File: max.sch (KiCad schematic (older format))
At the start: 48 parts, among them P4 ttyMAX2, P5 ttyMAX1, P6 ttyMAX0, SW2 gpio 8 9 10 11, U8 SG-210STF_16MHz, U9 MAX14830

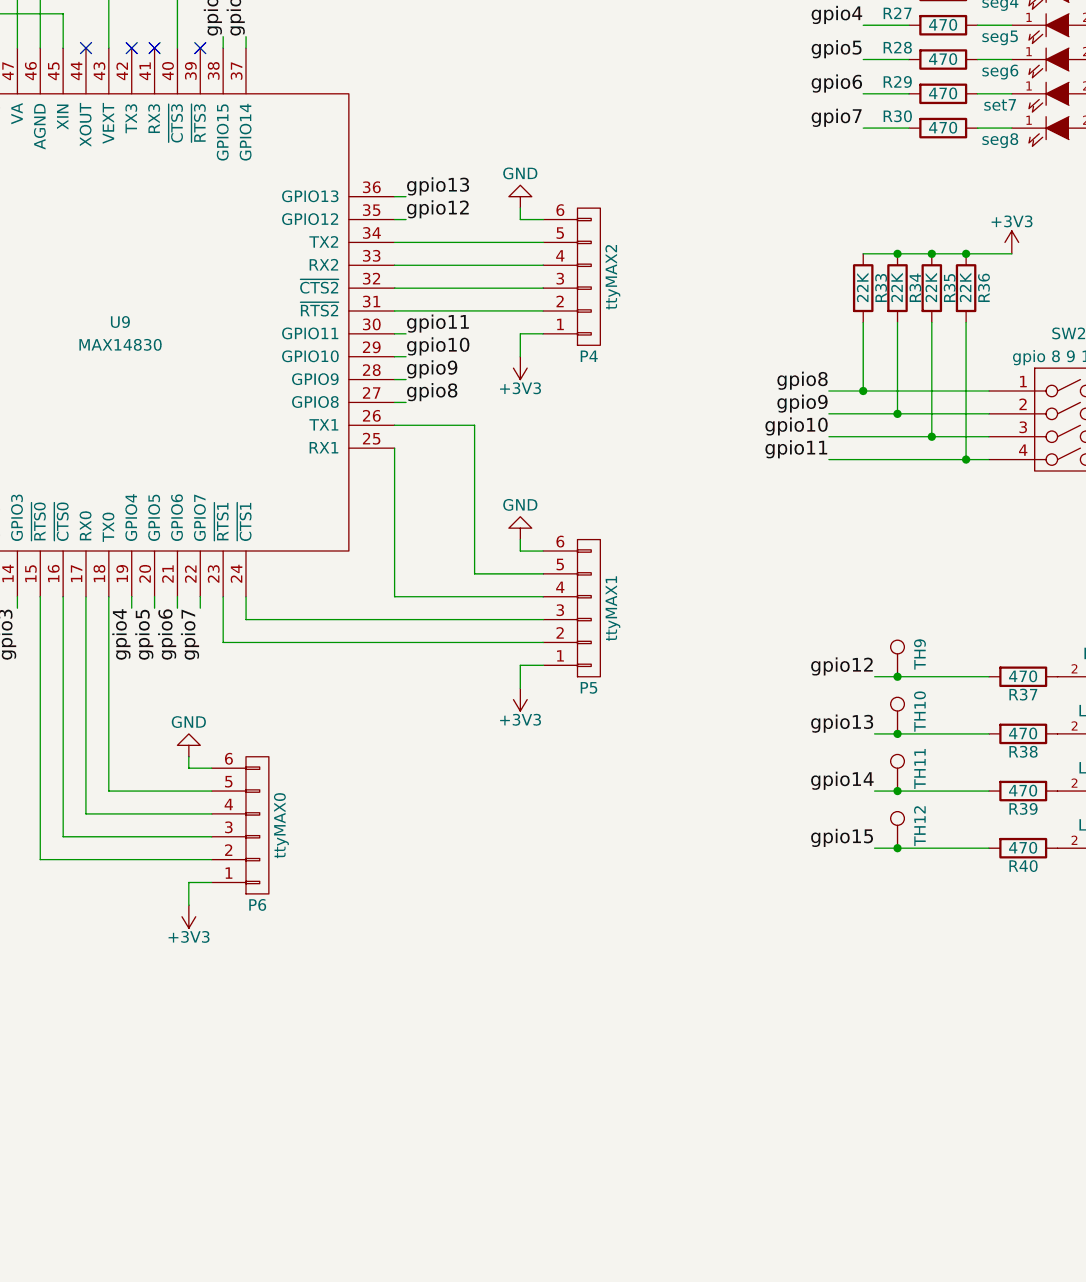
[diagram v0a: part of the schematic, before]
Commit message: Improved the pin comatibility to match with other ardupilot project.
Signed-off-by: Akira Tsukamoto <akira-t@s9.dion.ne.jp>
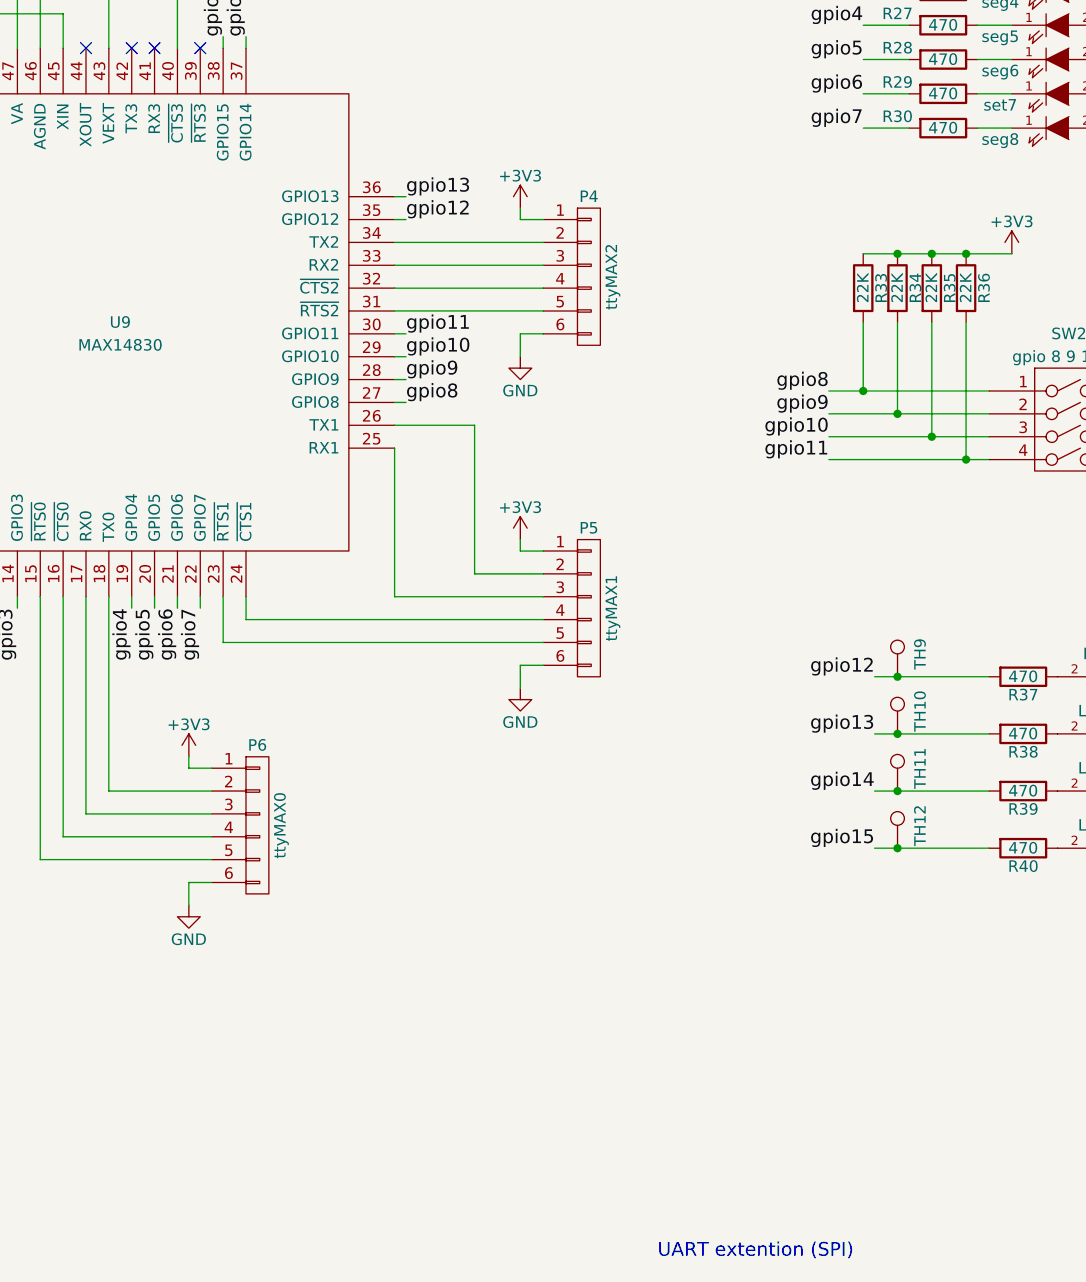
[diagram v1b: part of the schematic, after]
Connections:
- net at U9.15 (~RTS0): now also P6.5 (P5); no longer P6.2 (P2)
- net at U9.16 (~CTS0): now also P6.4 (P4); no longer P6.3 (P3)
- net at U9.17 (RX0): now also P6.3 (P3); no longer P6.4 (P4)
- net at U9.18 (TX0): now also P6.2 (P2); no longer P6.5 (P5)
- net at U9.23 (~RTS1): now also P5.5 (P5); no longer P5.2 (P2)
- net at U9.24 (~CTS1): now also P5.4 (P4); no longer P5.3 (P3)
- net at U9.25 (RX1): now also P5.3 (P3); no longer P5.4 (P4)
- net at U9.26 (TX1): now also P5.2 (P2); no longer P5.5 (P5)
- net at U9.31 (~RTS2): now also P4.5 (P5); no longer P4.2 (P2)
- net at U9.32 (~CTS2): now also P4.4 (P4); no longer P4.3 (P3)
- net at U9.33 (RX2): now also P4.3 (P3); no longer P4.4 (P4)
- net at U9.34 (TX2): now also P4.2 (P2); no longer P4.5 (P5)
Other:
- note added: "UART extention (SPI)"
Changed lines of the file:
@@
 F 3 "" H 7000 3200 60  0000 C CNN
 	1    7000 3200
-	1    0    0    1
+	1    0    0    -1
 $EndComp
 $Comp
 L GND #PWR042
 U 1 1 56F7B7A9
-P 6700 2900
-F 0 "#PWR042" H 6700 2650 50  0001 C CNN
-F 1 "GND" H 6700 2750 50  0000 C CNN
-F 2 "" H 6700 2900 60  0000 C CNN
-F 3 "" H 6700 2900 60  0000 C CNN
-	1    6700 2900
-	1    0    0    1
+P 6700 3550
+F 0 "#PWR042" H 6700 3300 50  0001 C CNN
+F 1 "GND" H 6700 3400 50  0000 C CNN
+F 2 "" H 6700 3550 60  0000 C CNN
+F 3 "" H 6700 3550 60  0000 C CNN
+	1    6700 3550
+	-1   0    0    -1
 $EndComp
 $Comp
@@
 F 3 "" H 7000 4650 60  0000 C CNN
 	1    7000 4650
-	1    0    0    1
+	1    0    0    -1
 $EndComp
 $Comp
 L GND #PWR043
 U 1 1 56F7B7BC
-P 6700 4350
-F 0 "#PWR043" H 6700 4100 50  0001 C CNN
-F 1 "GND" H 6700 4200 50  0000 C CNN
-F 2 "" H 6700 4350 60  0000 C CNN
-F 3 "" H 6700 4350 60  0000 C CNN
-	1    6700 4350
-	1    0    0    1
+P 6700 5000
+F 0 "#PWR043" H 6700 4750 50  0001 C CNN
+F 1 "GND" H 6700 4850 50  0000 C CNN
+F 2 "" H 6700 5000 60  0000 C CNN
+F 3 "" H 6700 5000 60  0000 C CNN
+	1    6700 5000
+	-1   0    0    -1
 $EndComp
 $Comp
@@
 F 3 "" H 5550 5600 60  0000 C CNN
 	1    5550 5600
-	1    0    0    1
-$EndComp
-$Comp
-L GND #PWR044
-U 1 1 56F7B7CF
-P 5250 5300
-F 0 "#PWR044" H 5250 5050 50  0001 C CNN
-F 1 "GND" H 5250 5150 50  0000 C CNN
-F 2 "" H 5250 5300 60  0000 C CNN
-F 3 "" H 5250 5300 60  0000 C CNN
-	1    5250 5300
-	1    0    0    1
+	1    0    0    -1
 $EndComp
 Text HLabel 1950 3050 0    60   Output ~ 0
@@
 $EndComp
 $Comp
-L GND #PWR045
+L GND #PWR044
 U 1 1 56FF154F
 P 9450 6000
-F 0 "#PWR045" H 9450 5750 50  0001 C CNN
+F 0 "#PWR044" H 9450 5750 50  0001 C CNN
 F 1 "GND" H 9450 5850 50  0000 C CNN
 F 2 "" H 9450 6000 60  0000 C CNN
@@
 $EndComp
 $Comp
-L GND #PWR046
+L GND #PWR045
 U 1 1 56FF190C
 P 9450 4450
-F 0 "#PWR046" H 9450 4200 50  0001 C CNN
+F 0 "#PWR045" H 9450 4200 50  0001 C CNN
 F 1 "GND" H 9450 4300 50  0000 C CNN
 F 2 "" H 9450 4450 60  0000 C CNN
@@
 NoConn ~ 4800 2200
 $Comp
-L GND #PWR047
+L GND #PWR046
 U 1 1 56FEE288
 P 3200 2250
-F 0 "#PWR047" H 3200 2000 50  0001 C CNN
+F 0 "#PWR046" H 3200 2000 50  0001 C CNN
 F 1 "GND" H 3200 2100 50  0000 C CNN
 F 2 "" H 3200 2250 50  0000 C CNN
@@
 $EndComp
 $Comp
-L GND #PWR048
+L GND #PWR047
 U 1 1 5705B8B8
 P 3750 2500
-F 0 "#PWR048" H 3750 2250 50  0001 C CNN
+F 0 "#PWR047" H 3750 2250 50  0001 C CNN
 F 1 "GND" H 3750 2350 50  0000 C CNN
 F 2 "" H 3750 2500 60  0000 C CNN
@@
 $EndComp
 $Comp
-L GND #PWR049
+L GND #PWR048
 U 1 1 57061BCC
 P 2900 4100
-F 0 "#PWR049" H 2900 3850 50  0001 C CNN
+F 0 "#PWR048" H 2900 3850 50  0001 C CNN
 F 1 "GND" H 2900 3950 50  0000 C CNN
 F 2 "" H 2900 4100 60  0000 C CNN
@@
 $EndComp
 $Comp
-L GND #PWR050
+L GND #PWR049
 U 1 1 57063190
 P 4300 1800
-F 0 "#PWR050" H 4300 1550 50  0001 C CNN
+F 0 "#PWR049" H 4300 1550 50  0001 C CNN
 F 1 "GND" H 4300 1650 50  0000 C CNN
 F 2 "" H 4300 1800 60  0000 C CNN
@@
 $EndComp
 $Comp
-L GND #PWR051
+L GND #PWR050
 U 1 1 5706380D
 P 4750 1800
-F 0 "#PWR051" H 4750 1550 50  0001 C CNN
+F 0 "#PWR050" H 4750 1550 50  0001 C CNN
 F 1 "GND" H 4750 1650 50  0000 C CNN
 F 2 "" H 4750 1800 60  0000 C CNN
@@
 	2550 3650 3750 3650
 $Comp
-L +3V3 #PWR052
+L +3V3 #PWR051
 U 1 1 57070627
 P 2350 1700
-F 0 "#PWR052" H 2350 1550 50  0001 C CNN
+F 0 "#PWR051" H 2350 1550 50  0001 C CNN
 F 1 "+3V3" H 2350 1840 50  0000 C CNN
 F 2 "" H 2350 1700 50  0000 C CNN
@@
 $EndComp
 $Comp
-L +3V3 #PWR053
+L +3V3 #PWR052
 U 1 1 5707075A
 P 2200 2600
-F 0 "#PWR053" H 2200 2450 50  0001 C CNN
+F 0 "#PWR052" H 2200 2450 50  0001 C CNN
 F 1 "+3V3" H 2200 2740 50  0000 C CNN
 F 2 "" H 2200 2600 50  0000 C CNN
@@
 $EndComp
 $Comp
-L +3V3 #PWR054
+L +3V3 #PWR053
 U 1 1 570707F5
 P 2500 2600
-F 0 "#PWR054" H 2500 2450 50  0001 C CNN
+F 0 "#PWR053" H 2500 2450 50  0001 C CNN
 F 1 "+3V3" H 2500 2740 50  0000 C CNN
 F 2 "" H 2500 2600 50  0000 C CNN
@@
 $EndComp
 $Comp
-L +3V3 #PWR055
+L +3V3 #PWR054
 U 1 1 5707088E
 P 2900 2600
-F 0 "#PWR055" H 2900 2450 50  0001 C CNN
+F 0 "#PWR054" H 2900 2450 50  0001 C CNN
 F 1 "+3V3" H 2900 2740 50  0000 C CNN
 F 2 "" H 2900 2600 50  0000 C CNN
@@
 $EndComp
 $Comp
-L +3V3 #PWR056
+L +3V3 #PWR055
 U 1 1 57070925
 P 4500 1250
-F 0 "#PWR056" H 4500 1100 50  0001 C CNN
+F 0 "#PWR055" H 4500 1100 50  0001 C CNN
 F 1 "+3V3" H 4500 1390 50  0000 C CNN
 F 2 "" H 4500 1250 50  0000 C CNN
 F 3 "" H 4500 1250 50  0000 C CNN
 	1    4500 1250
-	1    0    0    -1
-$EndComp
-$Comp
-L +3V3 #PWR057
-U 1 1 570709BC
-P 4900 1250
-F 0 "#PWR057" H 4900 1100 50  0001 C CNN
-F 1 "+3V3" H 4900 1390 50  0000 C CNN
-F 2 "" H 4900 1250 50  0000 C CNN
-F 3 "" H 4900 1250 50  0000 C CNN
-	1    4900 1250
-	1    0    0    -1
-$EndComp
-$Comp
-L +3V3 #PWR058
-U 1 1 57070AEA
-P 6700 3550
-F 0 "#PWR058" H 6700 3400 50  0001 C CNN
-F 1 "+3V3" H 6700 3690 50  0000 C CNN
-F 2 "" H 6700 3550 50  0000 C CNN
-F 3 "" H 6700 3550 50  0000 C CNN
-	1    6700 3550
-	1    0    0    1
-$EndComp
-$Comp
-L +3V3 #PWR059
-U 1 1 570715D1
-P 6700 5000
-F 0 "#PWR059" H 6700 4850 50  0001 C CNN
-F 1 "+3V3" H 6700 5140 50  0000 C CNN
-F 2 "" H 6700 5000 50  0000 C CNN
-F 3 "" H 6700 5000 50  0000 C CNN
-	1    6700 5000
-	1    0    0    1
-$EndComp
-$Comp
-L +3V3 #PWR060
-U 1 1 57072088
-P 5250 5950
-F 0 "#PWR060" H 5250 5800 50  0001 C CNN
-F 1 "+3V3" H 5250 6090 50  0000 C CNN
-F 2 "" H 5250 5950 50  0000 C CNN
-F 3 "" H 5250 5950 50  0000 C CNN
-	1    5250 5950
-	1    0    0    1
-$EndComp
-$Comp
-L +3V3 #PWR061
-U 1 1 570A6A75
-P 9500 1350
-F 0 "#PWR061" H 9500 1200 50  0001 C CNN
-F 1 "+3V3" H 9500 1490 50  0000 C CNN
-F 2 "" H 9500 1350 50  0000 C CNN
-F 3 "" H 9500 1350 50  0000 C CNN
-	1    9500 1350
-	1    0    0    -1
-$EndComp
-$Comp
-L +3V3 #PWR062
-U 1 1 570A6AE9
-P 8850 3100
-F 0 "#PWR062" H 8850 2950 50  0001 C CNN
-F 1 "+3V3" H 8850 3240 50  0000 C CNN
-F 2 "" H 8850 3100 50  0000 C CNN
-F 3 "" H 8850 3100 50  0000 C CNN
-	1    8850 3100
 	1    0    0    -1
 $EndComp
@@
 	5200 1750 6150 1750
 $Comp
-L GND #PWR063
+L GND #PWR056
 U 1 1 58DB9CD2
 P 6700 1800
-F 0 "#PWR063" H 6700 1550 50  0001 C CNN
+F 0 "#PWR056" H 6700 1550 50  0001 C CNN
 F 1 "GND" H 6700 1650 50  0000 C CNN
 F 2 "" H 6700 1800 50  0000 C CNN
@@
 Wire Wire Line
 	6700 1750 6700 1800
+Text Notes 7300 7500 0    60   ~ 0
+UART extention (SPI)
+$Comp
+L GND #PWR057
+U 1 1 5A32C449
+P 5250 5950
+F 0 "#PWR057" H 5250 5700 50  0001 C CNN
+F 1 "GND" H 5250 5800 50  0000 C CNN
+F 2 "" H 5250 5950 60  0000 C CNN
+F 3 "" H 5250 5950 60  0000 C CNN
+	1    5250 5950
+	-1   0    0    -1
+$EndComp
+$Comp
+L +3V3 #PWR?
+U 1 1 5A334123
+P 4900 1250
+F 0 "#PWR?" H 4900 1100 50  0001 C CNN
+F 1 "+3V3" H 4900 1390 50  0000 C CNN
+F 2 "" H 4900 1250 50  0000 C CNN
+F 3 "" H 4900 1250 50  0000 C CNN
+	1    4900 1250
+	1    0    0    -1
+$EndComp
+$Comp
+L +3V3 #PWR?
+U 1 1 5A3344BF
+P 9500 1350
+F 0 "#PWR?" H 9500 1200 50  0001 C CNN
+F 1 "+3V3" H 9500 1490 50  0000 C CNN
+F 2 "" H 9500 1350 50  0000 C CNN
+F 3 "" H 9500 1350 50  0000 C CNN
+	1    9500 1350
+	1    0    0    -1
+$EndComp
+$Comp
+L +3V3 #PWR?
+U 1 1 5A33473A
+P 8850 3100
+F 0 "#PWR?" H 8850 2950 50  0001 C CNN
+F 1 "+3V3" H 8850 3240 50  0000 C CNN
+F 2 "" H 8850 3100 50  0000 C CNN
+F 3 "" H 8850 3100 50  0000 C CNN
+	1    8850 3100
+	1    0    0    -1
+$EndComp
+$Comp
+L +3V3 #PWR?
+U 1 1 5A334C91
+P 6700 2900
+F 0 "#PWR?" H 6700 2750 50  0001 C CNN
+F 1 "+3V3" H 6700 3040 50  0000 C CNN
+F 2 "" H 6700 2900 50  0000 C CNN
+F 3 "" H 6700 2900 50  0000 C CNN
+	1    6700 2900
+	1    0    0    -1
+$EndComp
+$Comp
+L +3V3 #PWR?
+U 1 1 5A334EAD
+P 6700 4350
+F 0 "#PWR?" H 6700 4200 50  0001 C CNN
+F 1 "+3V3" H 6700 4490 50  0000 C CNN
+F 2 "" H 6700 4350 50  0000 C CNN
+F 3 "" H 6700 4350 50  0000 C CNN
+	1    6700 4350
+	1    0    0    -1
+$EndComp
+$Comp
+L +3V3 #PWR?
+U 1 1 5A334F79
+P 5250 5300
+F 0 "#PWR?" H 5250 5150 50  0001 C CNN
+F 1 "+3V3" H 5250 5440 50  0000 C CNN
+F 2 "" H 5250 5300 50  0000 C CNN
+F 3 "" H 5250 5300 50  0000 C CNN
+	1    5250 5300
+	1    0    0    -1
+$EndComp
 $EndSCHEMATC
